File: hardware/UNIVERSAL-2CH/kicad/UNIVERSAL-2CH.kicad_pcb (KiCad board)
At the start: 4 copper layers, 120 x 135 mm, 90 parts, among them J1 ACTUATOR_CH1_4P, J2 ACTUATOR_CH2_4P, J201 REED_A_OPEN_3V3_SIG_GND, J202 REED_A_CLOSED_3V3_SIG_GND, J203 REED_A_IN_PLACE_3V3_SIG_GND, J211 CAP_CS1_GND, J212 CAP_CS2_GND, J213 CAP_CS3_GND, J220 SWD_S1_3V3_DIO_CLK_NRST_GND, J230 LOGIC_12V_GND, J240 CANH_CANL_GND_SHIELD, U1 VNH5019A-E, U2 VNH5019A-E, U230 AMS1117-3V3, U250 25LC256_SOIC8_CARRIER_ID, U270 TLV6700DDCR_POWER_MONITOR

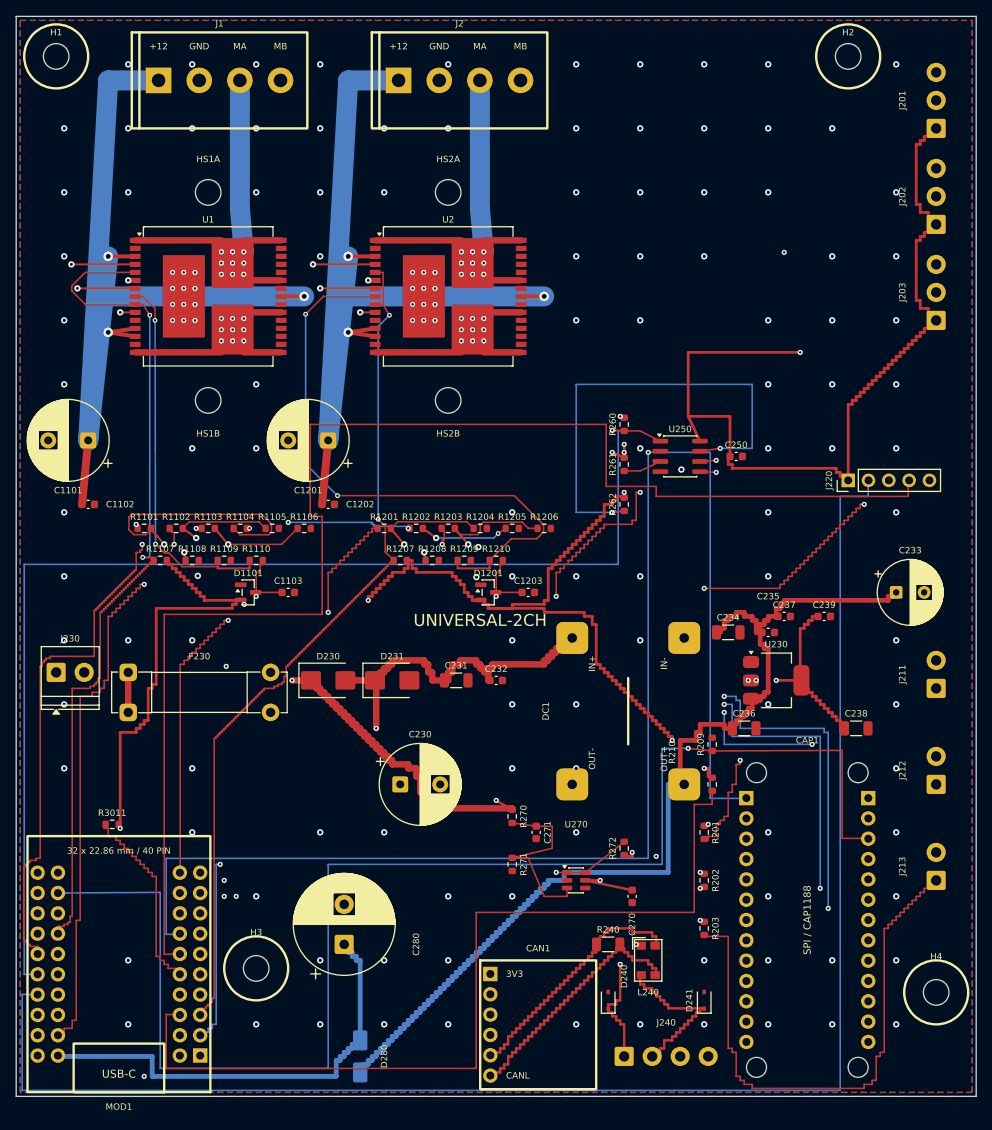
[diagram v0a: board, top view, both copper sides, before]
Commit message: Complete compact 2-channel PCB routing
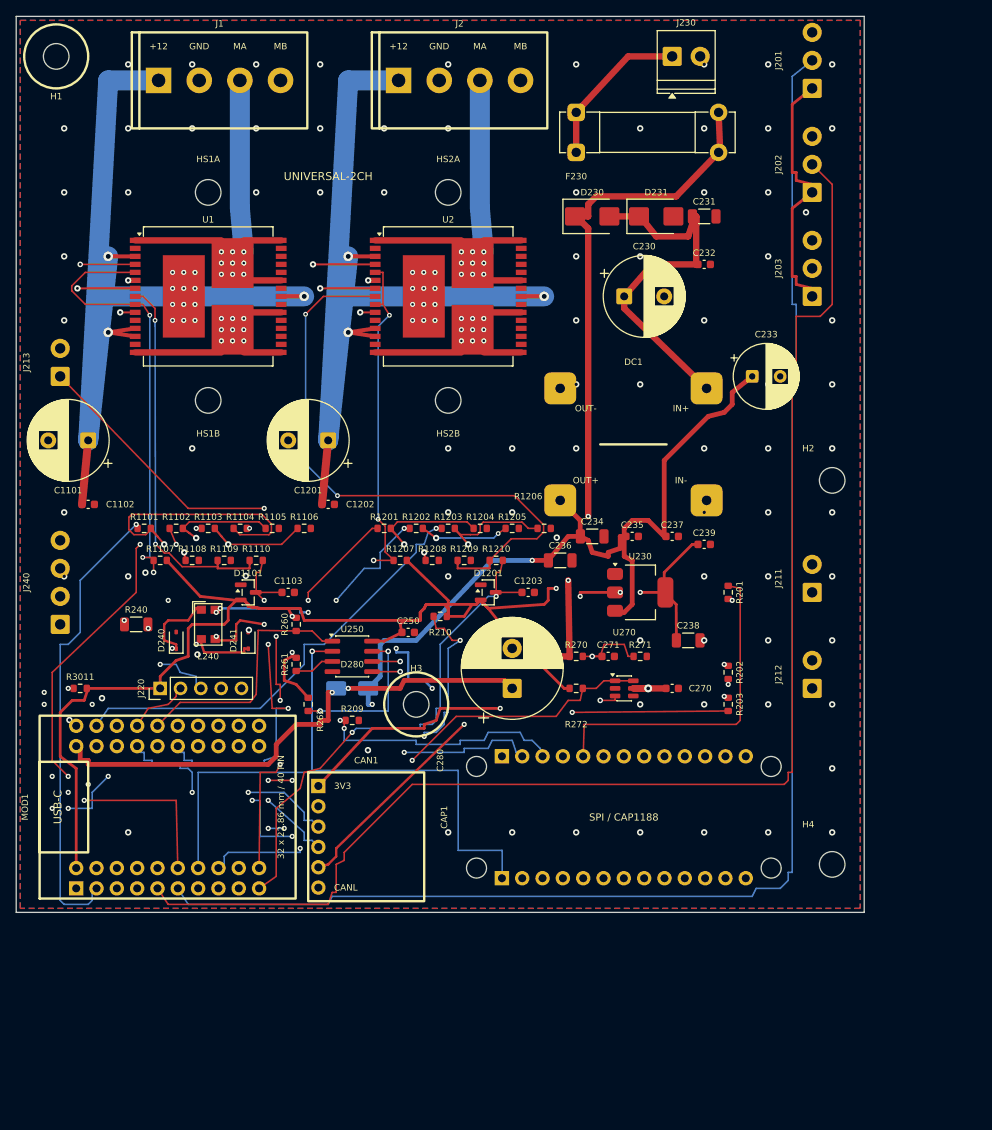
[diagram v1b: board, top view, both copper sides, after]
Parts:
- moved J213 126.3 mm to (5.50, 45.0)
- moved J230 108.9 mm to (82.0, 5.00)
- moved J220 89.8 mm to (18.0, 84.0)
- moved F230 89.6 mm to (70.0, 12.0)
- moved J240 88.8 mm to (5.50, 76.0), turned to 90 degrees
- moved D241 72.6 mm to (29.0, 78.0)
- moved R240 71.3 mm to (15.0, 76.0)
- moved D240 70.3 mm to (20.0, 78.0)
- moved L240 69.2 mm to (24.0, 76.0)
- moved C230 67.1 mm to (76.0, 35.0)
- moved D230 66.7 mm to (72.0, 25.0)
- moved D231 66.7 mm to (80.0, 25.0)
- moved C231 65.8 mm to (86.0, 25.0)
- moved C232 58.1 mm to (86.0, 31.0)
- moved DC1 53.0 mm to (66.0, 45.0), turned to 0 degrees
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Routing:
- net S1_SWDIO: track 196.0 -> 8.08 mm
- net S1_3V3: track 434.9 -> 266.3 mm, vias 12 -> 3
- net EEPROM_CS: track 151.0 -> 31.9 mm, vias 1 -> 0
- net S1_NRST: track 175.3 -> 65.3 mm, vias 0 -> 2
- net CAP_RESET: track 174.3 -> 68.2 mm, vias 1 -> 4
- net S1_SWCLK: track 165.9 -> 59.9 mm, vias 2 -> 4
- net CAP_MOSI: track 184.2 -> 83.0 mm
- net REED_A_IN_PLACE: track 205.7 -> 105.6 mm
- net CAP_CS: track 145.2 -> 54.5 mm, vias 0 -> 2
- net CH2_DIAG: track 120.8 -> 209.3 mm, vias 2 -> 3
- net CAP_MISO: track 179.4 -> 96.1 mm
- net CAP_C3_RAW: track 91.7 -> 17.2 mm, vias 3 -> 1
- net CAP_SCK: track 171.7 -> 100.8 mm
- net POWER_GOOD: track 121.2 -> 58.7 mm, vias 1 -> 3
- net CH2_PWM_MCU: track 118.0 -> 56.0 mm, vias 2 -> 1
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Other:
- board size 120 x 135 mm -> 106 x 112 mm
